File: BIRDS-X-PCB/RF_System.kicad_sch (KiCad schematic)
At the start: 39 parts, among them J501 60611002111501, U501 SX1276, U502 PE4259, U503 TXKTPCSANF-32

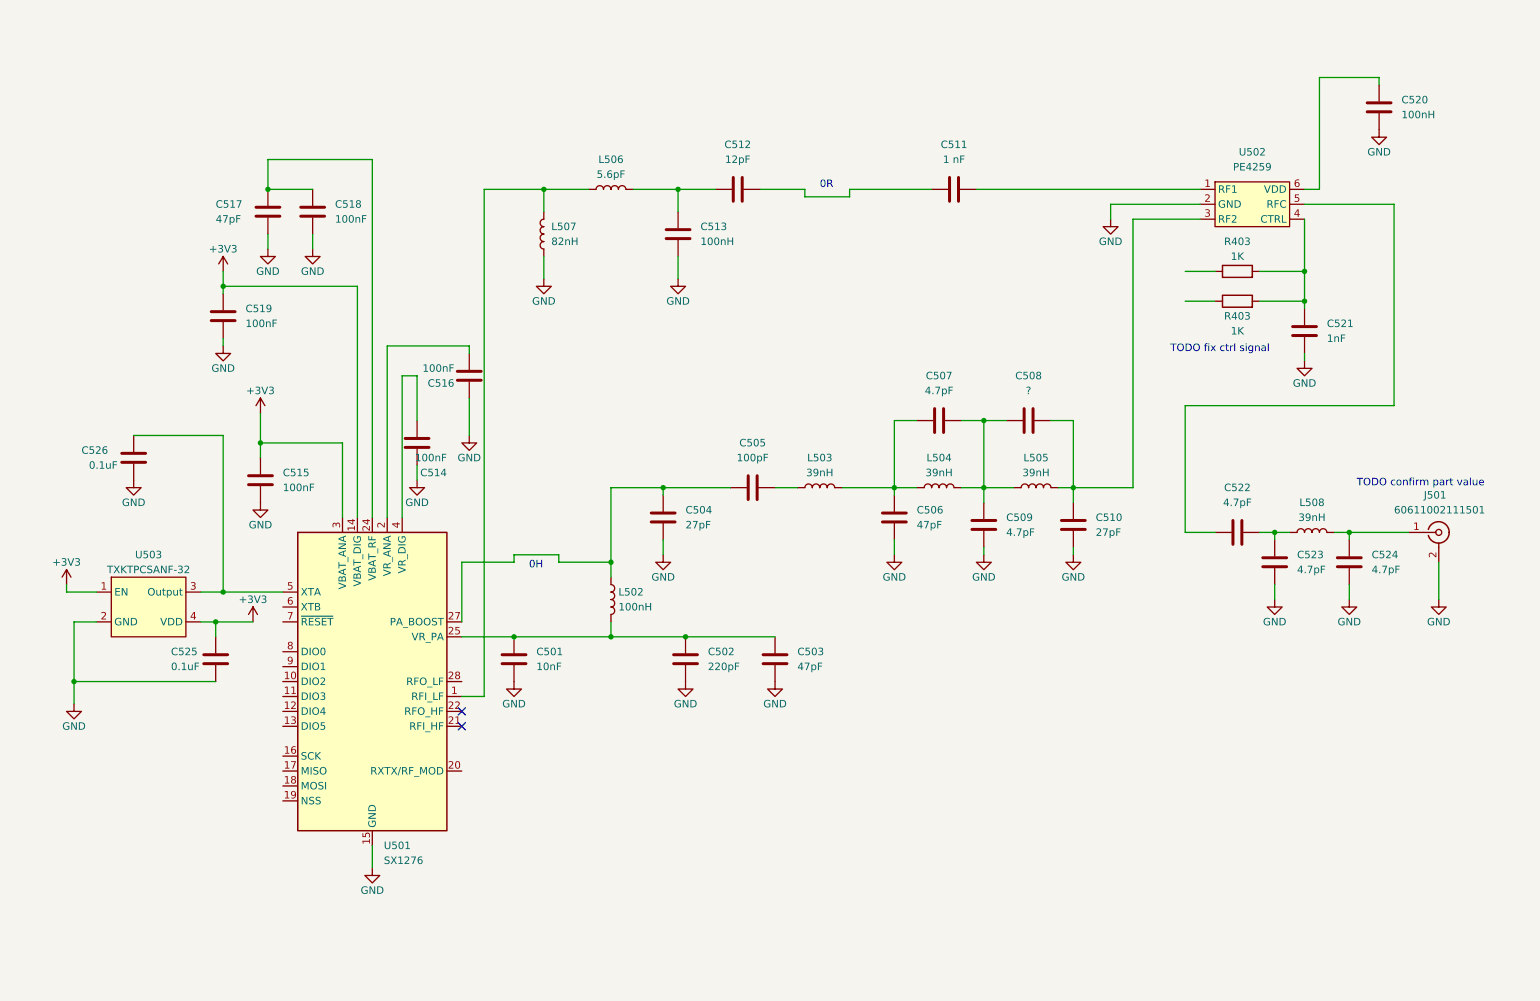
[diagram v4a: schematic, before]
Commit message: Add MCU assignments, RF annotations per ref design, heirarchal pins
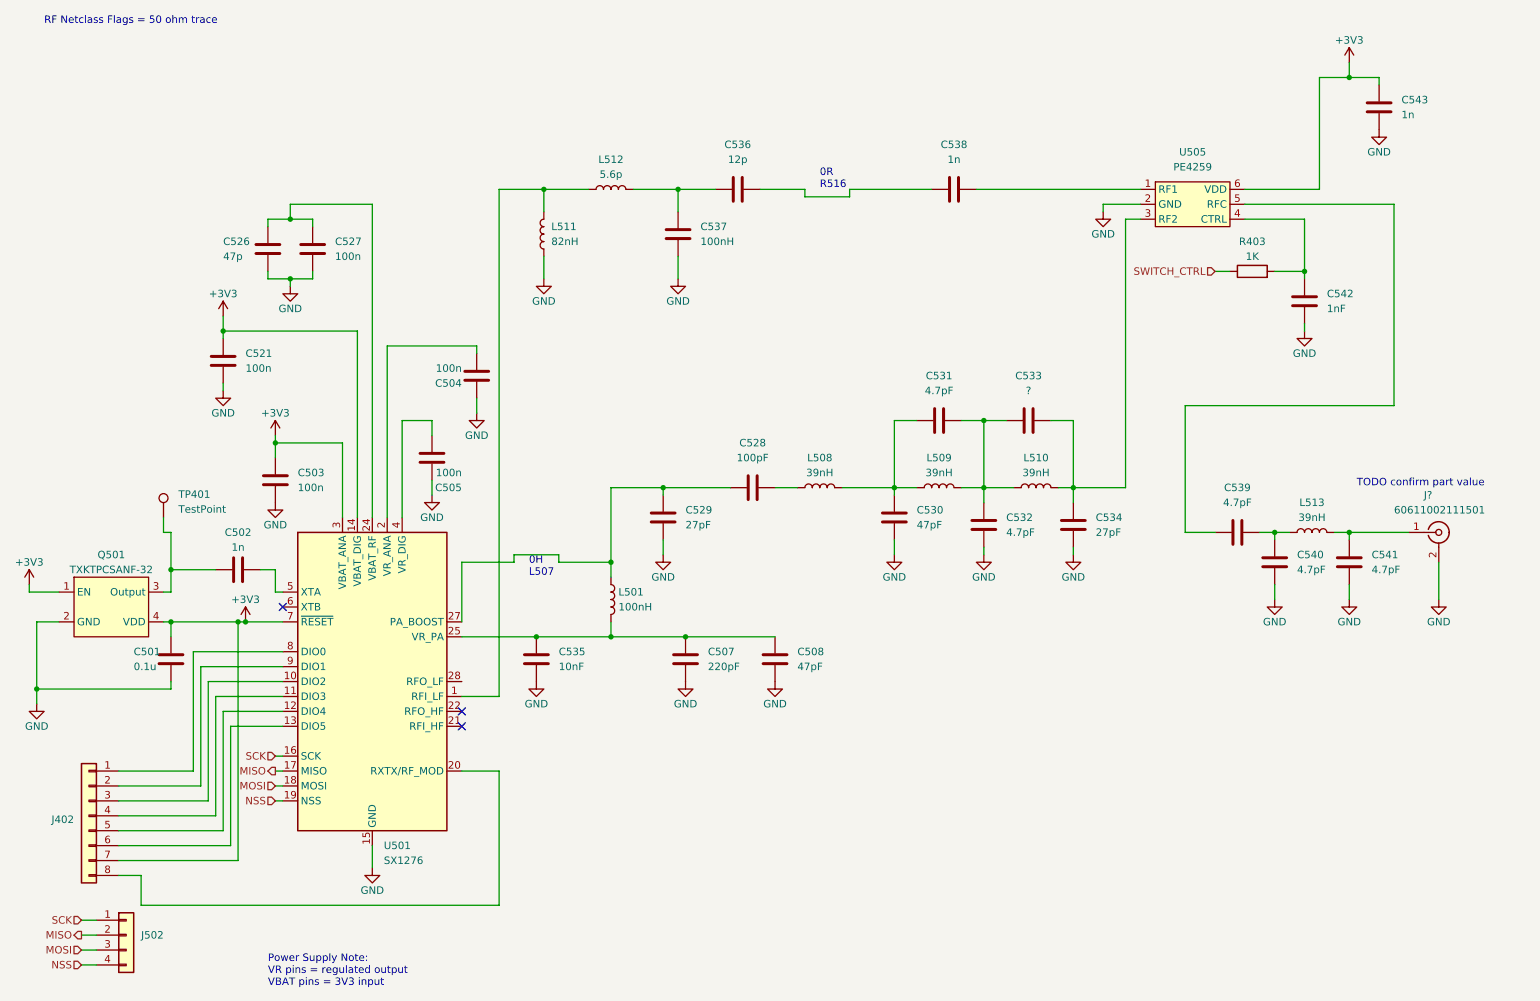
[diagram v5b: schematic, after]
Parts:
- removed C526: 0.1uF, Capacitor_SMD:C_0603_1608Metric_Pad1.08x0.95mm_HandSolder, symbol Device:C
- removed R403: 1K, Resistor_SMD:R_0603_1608Metric_Pad0.98x0.95mm_HandSolder, symbol Device:R
- added C502: 1n, Capacitor_SMD:C_0603_1608Metric_Pad1.08x0.95mm_HandSolder, symbol Device:C
- added J402: Conn_01x08, Connector_PinHeader_1.27mm:PinHeader_1x08_P1.27mm_Vertical, symbol Connector_Generic:Conn_01x08
- added J502: Conn_01x04, symbol Connector_Generic:Conn_01x04
- added TP401: TestPoint, TestPoint:TestPoint_Pad_D1.5mm, symbol Connector:TestPoint
- C501: renamed from C525; value 0.1uF -> 0.1u
- C503: renamed from C515; value 100nF -> 100n
- C504: renamed from C516; value 100nF -> 100n
- C505: renamed from C514; value 100nF -> 100n
- C521: renamed from C519; value 100nF -> 100n
- C526: renamed from C517; value 47pF -> 47p
- C527: renamed from C518; value 100nF -> 100n
- C536: renamed from C512; value 12pF -> 12p
- C538: renamed from C511; value 1 nF -> 1n
- C543: renamed from C520; value 100nH -> 1n
- L512: renamed from L506; value 5.6pF -> 5.6p
- renumbered C502 to C507, C503 to C508, C505 to C528, C504 to C529, C506 to C530, C507 to C531, C509 to C532, C508 to C533, C510 to C534, C501 to C535, C513 to C537, C522 to C539, C523 to C540, C524 to C541, C521 to C542, J501 to J?, L502 to L501, L503 to L508, L504 to L509, L505 to L510, L507 to L511, L508 to L513, U503 to Q501, U502 to U505
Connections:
- net +3V3: now also C543.2, U501.7 (~{RESET}), U505.6 (VDD), J402.7 (Pin_7)
- net at Q501.3 (Output): now also C502.1, TP401.1; no longer U501.5 (XTA)
- net SWITCH_CTRL: now reaches R403.1
- net at U501.10 (DIO2): now also J402.3 (Pin_3)
- net at U501.11 (DIO3): now also J402.4 (Pin_4)
- net at U501.12 (DIO4): now also J402.5 (Pin_5)
- net at U501.13 (DIO5): now also J402.6 (Pin_6)
- net SCK: now reaches U501.16 (SCK)
- net SCK: now also J502.1 (Pin_1)
- net MISO: now reaches U501.17 (MISO)
- net MISO: now also J502.2 (Pin_2)
- net MOSI: now reaches U501.18 (MOSI)
- net MOSI: now also J502.3 (Pin_3)
- net NSS: now reaches U501.19 (NSS)
- net NSS: now also J502.4 (Pin_4)
- net at U501.20 (RXTX/RF_MOD): now also J402.8 (Pin_8)
- net at U501.8 (DIO0): now also J402.1 (Pin_1)
- net at U501.9 (DIO1): now also J402.2 (Pin_2)
- new net: C502.2, U501.5 (XTA)
- no-connect marks 2 -> 3
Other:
- note added: "0H L507"
- note added: "0R R516"
- note added: "Power Supply Note: VR pins = regulated output VBAT pins = 3V3 input"
- note added: "RF Netclass Flags = 50 ohm trace"
- note removed: "0H"
- note removed: "0R"
- note removed: "TODO fix ctrl signal"
- moved on the sheet: C501, C503, C504, C505, C521, C526, C527, C535, C542, Q501, R403, U505

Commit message: Finish most routing
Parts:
- J502: footprint (none) -> Connector_PinHeader_1.27mm:PinHeader_1x04_P1.27mm_Vertical
- TP401: footprint TestPoint:TestPoint_Pad_D1.5mm -> TestPoint:TestPoint_Pad_D1.0mm
- gave numbers to parts that had none: 1
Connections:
- net +3V3: now also C526.1, C527.1, U501.24 (VBAT_RF); no longer J402.7 (Pin_7), U501.7 (~{RESET})
- new net: J402.7 (Pin_7), U501.7 (~{RESET})
- no-connect marks 3 -> 4

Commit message: Update pins and LCSC part numbers
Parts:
- removed C537: 100nH, Capacitor_SMD:C_0603_1608Metric_Pad1.08x0.95mm_HandSolder, symbol Device:C
- removed L512: 5.6p, Inductor_SMD:L_0603_1608Metric_Pad1.05x0.95mm_HandSolder, symbol Device:L
- added C590: 5.6p, Capacitor_SMD:C_0603_1608Metric_Pad1.08x0.95mm_HandSolder, symbol Device:C
- added L590: 100n, Inductor_SMD:L_0603_1608Metric_Pad1.05x0.95mm_HandSolder, symbol Device:L
- U505: LCSC (none) -> C470892
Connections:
- net GND: now also L590.1
- net at L511.2, U501.1 (RFI_LF): now also C590.1
- net at C536.1: now also C590.2, L590.2
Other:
- note added: "C590 was formerly labelled L512"
- note added: "L590 was formerly labelled C537"
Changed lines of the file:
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@@
+    (effects (font (size 1.27 1.27)) (justify left bottom))
+  )
+  (text "L590 was formerly labelled C537" (at 128.27 59.69 0)
     (effects (font (size 1.27 1.27)) (justify left bottom))
   )
   (text "RF Netclass Flags = 50 ohm trace" (at 19.05 19.05 0)
+    (effects (font (size 1.27 1.27)) (justify left bottom))
+  )
+  (text "C590 was formerly\nlabelled L512" (at 109.22 36.83 0)
     (effects (font (size 1.27 1.27)) (justify left bottom))
   )
@@
     )
   )
-  (symbol (lib_id "Device:L") (at 115.57 46.99 90) (unit 1)
-    (in_bom yes) (on_board yes) (dnp no) (fields_autoplaced)
-    (property "Reference" "L512" (at 115.57 41.91 90)
-      (effects (font (size 1.27 1.27)))
-    )
-    (property "Value" "5.6p" (at 115.57 44.45 90)
-      (effects (font (size 1.27 1.27)))
-    )
-    (property "Footprint" "Inductor_SMD:L_0603_1608Metric_Pad1.05x0.95mm_HandSolder" (at 115.57 46.99 0)
+  (symbol (lib_id "Device:C") (at 115.57 46.99 90) (unit 1)
+    (in_bom yes) (on_board yes) (dnp no) (fields_autoplaced)
+    (property "Reference" "C590" (at 115.57 39.37 90)
+      (effects (font (size 1.27 1.27)))
+    )
+    (property "Value" "5.6p" (at 115.57 41.91 90)
+      (effects (font (size 1.27 1.27)))
+    )
+    (property "Footprint" "Capacitor_SMD:C_0603_1608Metric_Pad1.08x0.95mm_HandSolder" (at 119.38 46.0248 0)
       (effects (font (size 1.27 1.27)) hide)
     )
@@
       (project "BIRDS-X-PCB"
         (path "/c2796b15-795a-4d6e-ad4b-0ba87ded4bc9/245c031a-1c72-4f7a-bf07-271990525459"
-          (reference "L512") (unit 1)
+          (reference "C590") (unit 1)
         )
       )
@@
         (path "/c2796b15-795a-4d6e-ad4b-0ba87ded4bc9/245c031a-1c72-4f7a-bf07-271990525459"
           (reference "#PWR0102") (unit 1)
-        )
-      )
-    )
-  )
-  (symbol (lib_id "Device:C") (at 127 54.61 180) (unit 1)
-    (in_bom yes) (on_board yes) (dnp no) (fields_autoplaced)
-    (property "Reference" "C537" (at 130.81 53.34 0)
-      (effects (font (size 1.27 1.27)) (justify right))
-    )
-    (property "Value" "100nH" (at 130.81 55.88 0)
-      (effects (font (size 1.27 1.27)) (justify right))
-    )
-    (property "Footprint" "Capacitor_SMD:C_0603_1608Metric_Pad1.08x0.95mm_HandSolder" (at 126.0348 50.8 0)
-      (effects (font (size 1.27 1.27)) hide)
-    )
-    (property "Datasheet" "~" (at 127 54.61 0)
-      (effects (font (size 1.27 1.27)) hide)
-    )
-    (pin "1")
-    (pin "2")
-    (instances
-      (project "BIRDS-X-PCB"
-        (path "/c2796b15-795a-4d6e-ad4b-0ba87ded4bc9/245c031a-1c72-4f7a-bf07-271990525459"
-          (reference "C537") (unit 1)
         )
       )
@@
       (effects (font (size 1.27 1.27)) hide)
     )
+    (property "LCSC" "C470892" (at 214.63 49.53 0)
+      (effects (font (size 1.27 1.27)) hide)
+    )
     (pin "1")
     (pin "2")
@@
         )
       )
+    )
+  )
+  (symbol (lib_id "Device:L") (at 127 54.61 180) (unit 1)
+    (in_bom yes) (on_board yes) (dnp no) (fields_autoplaced)
+    (property "Reference" "L590" (at 128.27 53.34 0)
+      (effects (font (size 1.27 1.27)) (justify right))
+    )
+    (property "Value" "100n" (at 128.27 55.88 0)
+      (effects (font (size 1.27 1.27)) (justify right))
+    )
+    (property "Footprint" "Inductor_SMD:L_0603_1608Metric_Pad1.05x0.95mm_HandSolder" (at 127 54.61 0)
+      (effects (font (size 1.27 1.27)) hide)
+    )
+    (property "Datasheet" "~" (at 127 54.61 0)
+      (effects (font (size 1.27 1.27)) hide)
+    )
+    (pin "1")
+    (pin "2")
+    (instances
+      (project "BIRDS-X-PCB"
+        (path "/c2796b15-795a-4d6e-ad4b-0ba87ded4bc9/245c031a-1c72-4f7a-bf07-271990525459"
+          (reference "L590") (unit 1)
+        )
+      )

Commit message: Add files via upload
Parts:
- C528: value 100pF -> 130pF
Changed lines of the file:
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@@
       (effects (font (size 1.27 1.27)))
     )
-    (property "Value" "100pF" (at 139.7 92.71 90)
+    (property "Value" "130pF" (at 139.7 92.71 90)
       (effects (font (size 1.27 1.27)))
     )
